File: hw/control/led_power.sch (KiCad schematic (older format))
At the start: 25 parts, among them Q1001 BC807, Q1002 BC817, U801 LM2678T-ADJ

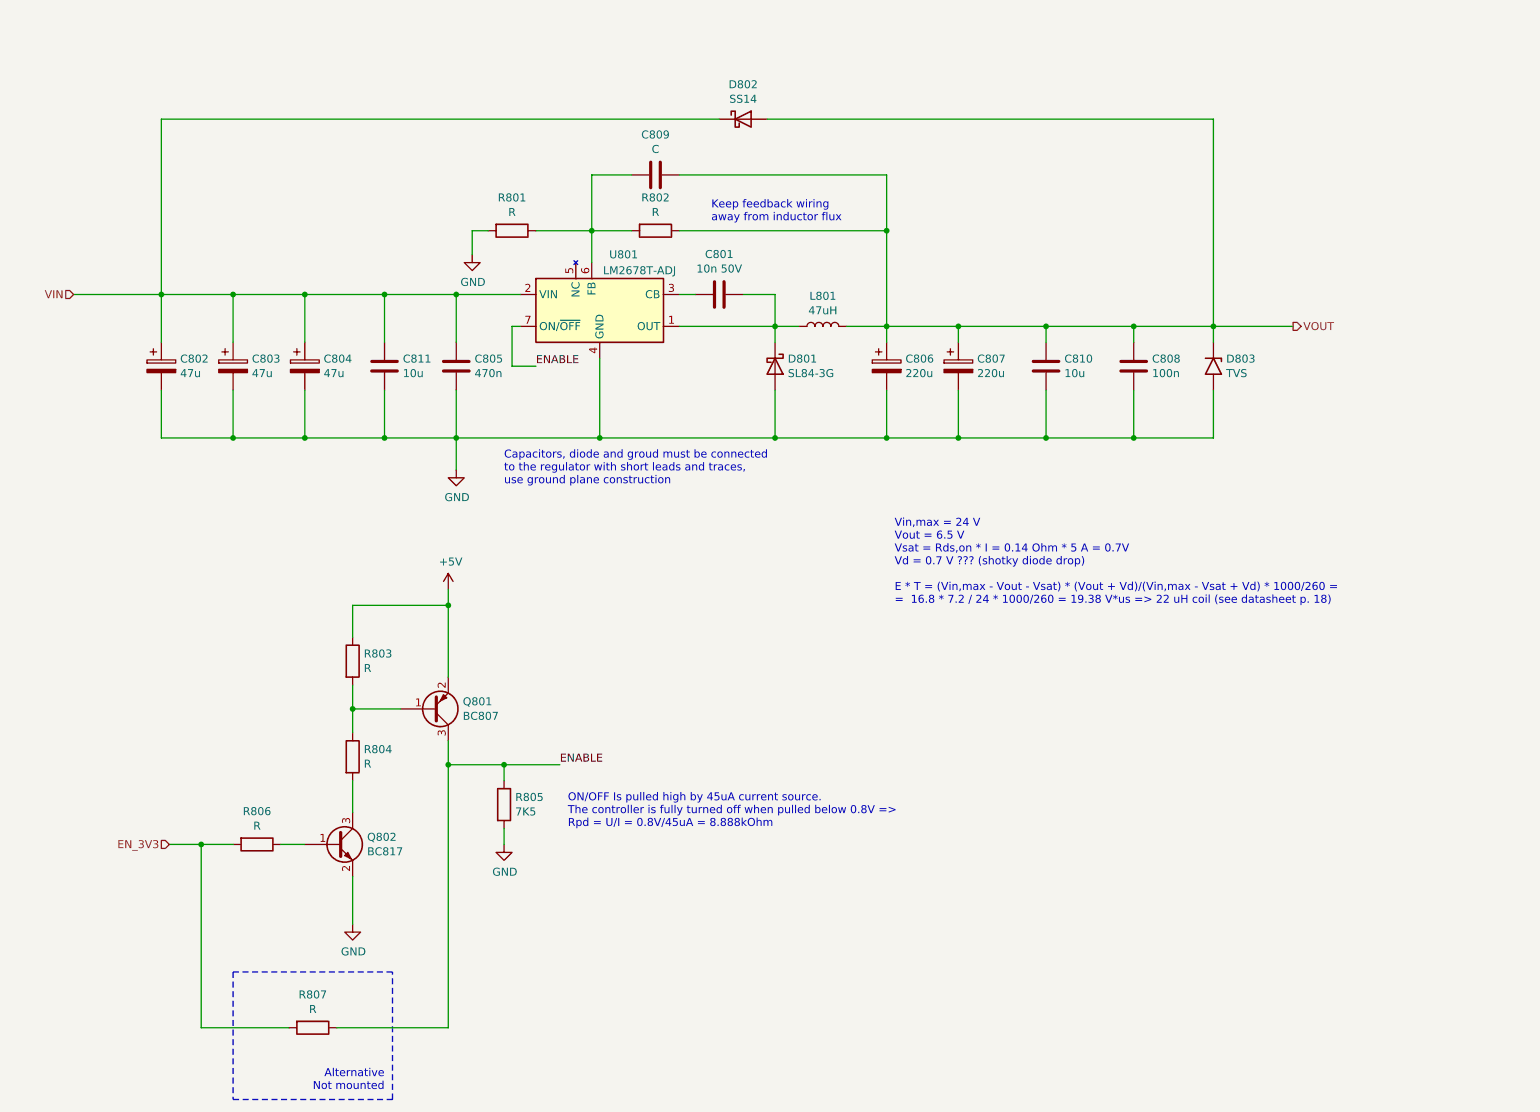
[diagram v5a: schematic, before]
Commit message: [hw] Add 5V supply layout
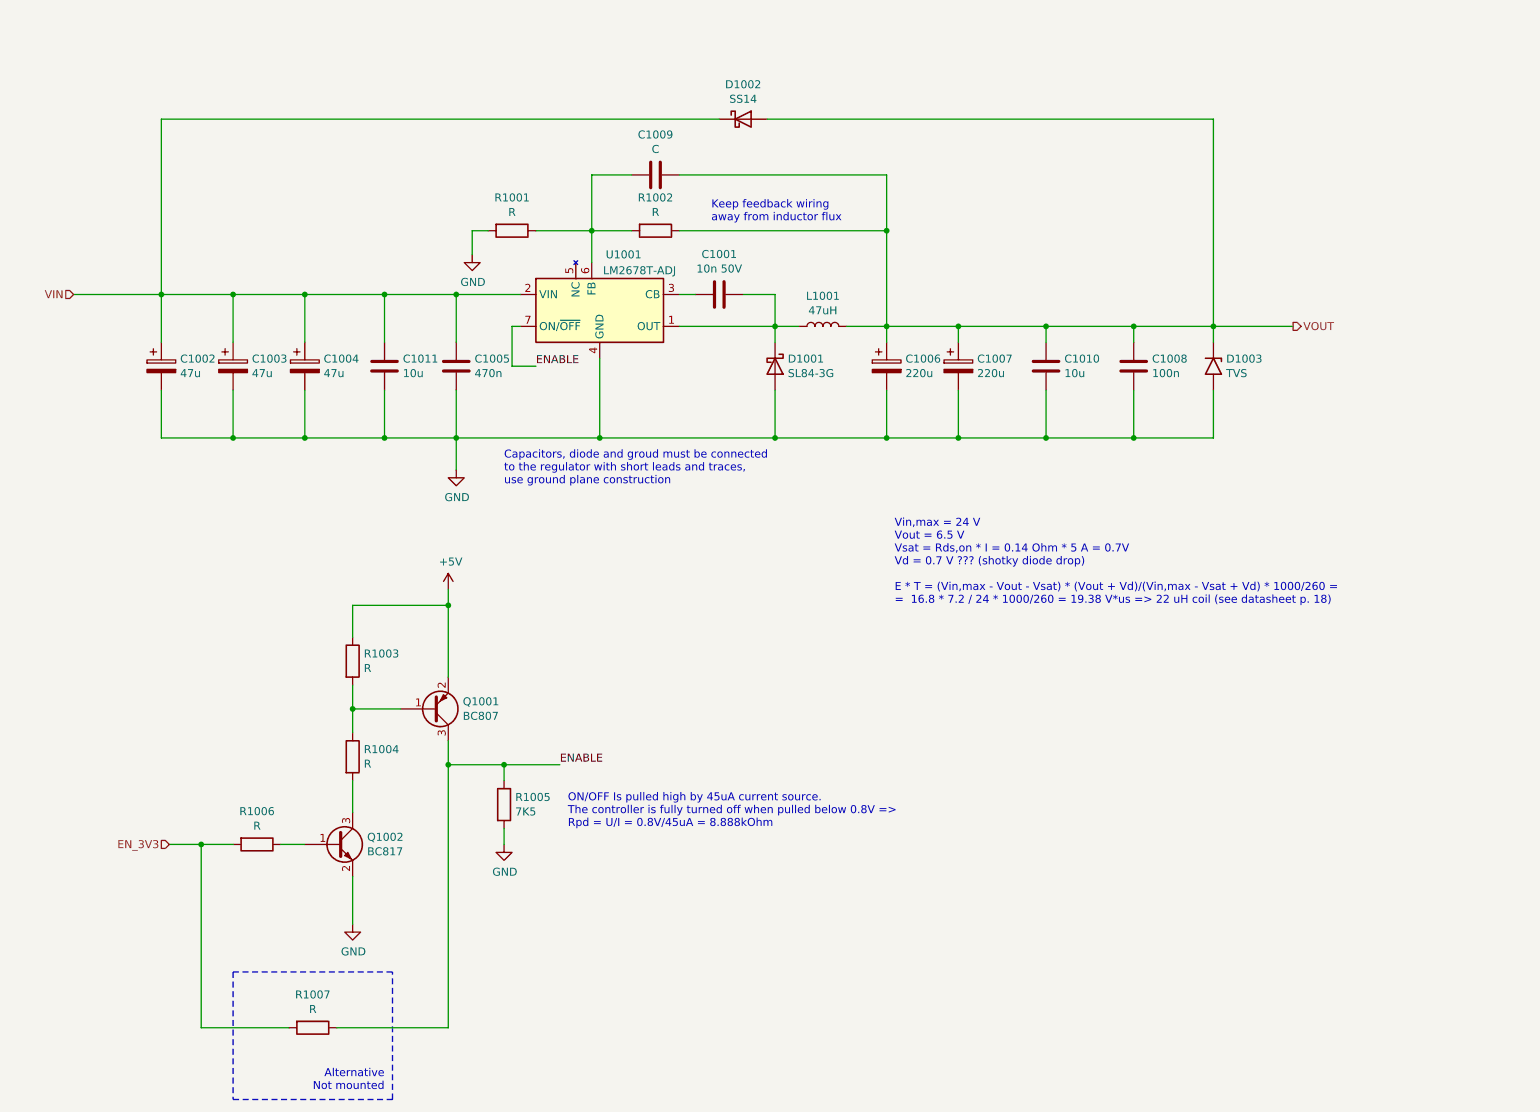
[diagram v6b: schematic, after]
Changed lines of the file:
@@
 AR Path="/614AB031/6145ECF0" Ref="U801"  Part="1"
 AR Path="/614AE8DA/6145ECF0" Ref="U1001"  Part="1"
-F 0 "U801" H 5550 2750 50  0000 C CNN
+F 0 "U1001" H 5550 2750 50  0000 C CNN
 F 1 "LM2678T-ADJ" H 5650 2650 50  0000 C CNN
 F 2 "Package_TO_SOT_THT:TO-220-7_P2.54x3.7mm_StaggerOdd_Lead3.8mm_Vertical" H 5450 2150 50  0001 L CIN
@@
 AR Path="/614AB031/6145FC0F" Ref="C801"  Part="1"
 AR Path="/614AE8DA/6145FC0F" Ref="C1001"  Part="1"
-F 0 "C801" V 5898 2300 50  0000 C CNN
+F 0 "C1001" V 5898 2300 50  0000 C CNN
 F 1 "10n 50V" V 5989 2300 50  0000 C CNN
 F 2 "Capacitor_SMD:C_0805_2012Metric_Pad1.18x1.45mm_HandSolder" H 6188 2150 50  0001 C CNN
@@
 AR Path="/614AB031/61460B18" Ref="#PWR0802"  Part="1"
 AR Path="/614AE8DA/61460B18" Ref="#PWR01002"  Part="1"
-F 0 "#PWR0802" H 4500 3150 50  0001 C CNN
+F 0 "#PWR01002" H 4500 3150 50  0001 C CNN
 F 1 "GND" H 4505 3227 50  0000 C CNN
 F 2 "" H 4500 3400 50  0001 C CNN
@@
 AR Path="/614AE8DA/61461C6E" Ref="D1001"  Part="1"
 AR Path="/614AB031/61461C6E" Ref="D801"  Part="1"
-F 0 "D801" V 6454 2830 50  0000 L CNN
+F 0 "D1001" V 6454 2830 50  0000 L CNN
 F 1 "SL84-3G" V 6545 2830 50  0000 L CNN
 F 2 "Diode_SMD:D_SMC_Handsoldering" H 6500 2750 50  0001 C CNN
@@
 AR Path="/614AE8DA/61462D51" Ref="L1001"  Part="1"
 AR Path="/614AB031/61462D51" Ref="L801"  Part="1"
-F 0 "L801" V 6990 2500 50  0000 C CNN
+F 0 "L1001" V 6990 2500 50  0000 C CNN
 F 1 "47uH" V 6899 2500 50  0000 C CNN
 F 2 "Inductor_THT:L_Toroid_Vertical_L22.4mm_W10.2mm_P7.90mm_Vishay_TJ4" H 6800 2500 50  0001 C CNN
@@
 AR Path="/614AE8DA/61463CC3" Ref="C1006"  Part="1"
 AR Path="/614AB031/61463CC3" Ref="C806"  Part="1"
-F 0 "C806" H 7318 2796 50  0000 L CNN
+F 0 "C1006" H 7318 2796 50  0000 L CNN
 F 1 "220u" H 7318 2705 50  0000 L CNN
 F 2 "Capacitor_THT:CP_Radial_D8.0mm_P3.50mm" H 7238 2600 50  0001 C CNN
@@
 AR Path="/614AE8DA/6146511A" Ref="C1007"  Part="1"
 AR Path="/614AB031/6146511A" Ref="C807"  Part="1"
-F 0 "C807" H 7768 2796 50  0000 L CNN
+F 0 "C1007" H 7768 2796 50  0000 L CNN
 F 1 "220u" H 7768 2705 50  0000 L CNN
 F 2 "Capacitor_THT:CP_Radial_D8.0mm_P3.50mm" H 7688 2600 50  0001 C CNN
@@
 AR Path="/614AE8DA/61465477" Ref="C1004"  Part="1"
 AR Path="/614AB031/61465477" Ref="C804"  Part="1"
-F 0 "C804" H 3668 2796 50  0000 L CNN
+F 0 "C1004" H 3668 2796 50  0000 L CNN
 F 1 "47u" H 3668 2705 50  0000 L CNN
 F 2 "Capacitor_THT:CP_Radial_D8.0mm_P3.50mm" H 3588 2600 50  0001 C CNN
@@
 AR Path="/614AE8DA/614679D1" Ref="C1003"  Part="1"
 AR Path="/614AB031/614679D1" Ref="C803"  Part="1"
-F 0 "C803" H 3218 2796 50  0000 L CNN
+F 0 "C1003" H 3218 2796 50  0000 L CNN
 F 1 "47u" H 3218 2705 50  0000 L CNN
 F 2 "Capacitor_THT:CP_Radial_D8.0mm_P3.50mm" H 3138 2600 50  0001 C CNN
@@
 AR Path="/614AE8DA/61467CFC" Ref="C1002"  Part="1"
 AR Path="/614AB031/61467CFC" Ref="C802"  Part="1"
-F 0 "C802" H 2768 2796 50  0000 L CNN
+F 0 "C1002" H 2768 2796 50  0000 L CNN
 F 1 "47u" H 2768 2705 50  0000 L CNN
 F 2 "Capacitor_THT:CP_Radial_D8.0mm_P3.50mm" H 2688 2600 50  0001 C CNN
@@
 AR Path="/614AE8DA/614681BF" Ref="C1005"  Part="1"
 AR Path="/614AB031/614681BF" Ref="C805"  Part="1"
-F 0 "C805" H 4615 2796 50  0000 L CNN
+F 0 "C1005" H 4615 2796 50  0000 L CNN
 F 1 "470n" H 4615 2705 50  0000 L CNN
 F 2 "Capacitor_SMD:C_0805_2012Metric_Pad1.18x1.45mm_HandSolder" H 4538 2600 50  0001 C CNN
@@
 AR Path="/614AE8DA/6147393D" Ref="R1002"  Part="1"
 AR Path="/614AB031/6147393D" Ref="R802"  Part="1"
-F 0 "R802" V 5543 1900 50  0000 C CNN
+F 0 "R1002" V 5543 1900 50  0000 C CNN
 F 1 "R" V 5634 1900 50  0000 C CNN
 F 2 "Resistor_SMD:R_0805_2012Metric_Pad1.20x1.40mm_HandSolder" V 5680 1900 50  0001 C CNN
@@
 AR Path="/614AE8DA/61475A47" Ref="R1001"  Part="1"
 AR Path="/614AB031/61475A47" Ref="R801"  Part="1"
-F 0 "R801" V 4643 1900 50  0000 C CNN
+F 0 "R1001" V 4643 1900 50  0000 C CNN
 F 1 "R" V 4734 1900 50  0000 C CNN
 F 2 "Resistor_SMD:R_0805_2012Metric_Pad1.20x1.40mm_HandSolder" V 4780 1900 50  0001 C CNN
@@
 AR Path="/614AE8DA/61477A40" Ref="#PWR01001"  Part="1"
 AR Path="/614AB031/61477A40" Ref="#PWR0801"  Part="1"
-F 0 "#PWR0801" H 4600 1800 50  0001 C CNN
+F 0 "#PWR01001" H 4600 1800 50  0001 C CNN
 F 1 "GND" H 4605 1877 50  0000 C CNN
 F 2 "" H 4600 2050 50  0001 C CNN
@@
 AR Path="/614AE8DA/6147DB7E" Ref="R1006"  Part="1"
 AR Path="/614AB031/6147DB7E" Ref="R806"  Part="1"
-F 0 "R806" V 3043 5750 50  0000 C CNN
+F 0 "R1006" V 3043 5750 50  0000 C CNN
 F 1 "R" V 3134 5750 50  0000 C CNN
 F 2 "Resistor_SMD:R_0805_2012Metric_Pad1.20x1.40mm_HandSolder" V 3180 5750 50  0001 C CNN
@@
 AR Path="/614AE8DA/6147EFCD" Ref="Q1002"  Part="1"
 AR Path="/614AB031/6147EFCD" Ref="Q802"  Part="1"
-F 0 "Q802" H 3941 5796 50  0000 L CNN
+F 0 "Q1002" H 3941 5796 50  0000 L CNN
 F 1 "BC817" H 3941 5705 50  0000 L CNN
 F 2 "Package_TO_SOT_SMD:SOT-23_Handsoldering" H 3950 5850 50  0001 C CNN
@@
 AR Path="/614AE8DA/61480A0D" Ref="Q1001"  Part="1"
 AR Path="/614AB031/61480A0D" Ref="Q801"  Part="1"
-F 0 "Q801" H 4541 4854 50  0000 L CNN
+F 0 "Q1001" H 4541 4854 50  0000 L CNN
 F 1 "BC807" H 4541 4945 50  0000 L CNN
 F 2 "Package_TO_SOT_SMD:SOT-23_Handsoldering" H 4550 5000 50  0001 C CNN
@@
 AR Path="/614AE8DA/6148128F" Ref="R1004"  Part="1"
 AR Path="/614AB031/6148128F" Ref="R804"  Part="1"
-F 0 "R804" H 3920 5246 50  0000 L CNN
+F 0 "R1004" H 3920 5246 50  0000 L CNN
 F 1 "R" H 3920 5155 50  0000 L CNN
 F 2 "Resistor_SMD:R_0805_2012Metric_Pad1.20x1.40mm_HandSolder" V 3780 5200 50  0001 C CNN
@@
 AR Path="/614AE8DA/614817B0" Ref="R1003"  Part="1"
 AR Path="/614AB031/614817B0" Ref="R803"  Part="1"
-F 0 "R803" H 3920 4646 50  0000 L CNN
+F 0 "R1003" H 3920 4646 50  0000 L CNN
 F 1 "R" H 3920 4555 50  0000 L CNN
 F 2 "Resistor_SMD:R_0805_2012Metric_Pad1.20x1.40mm_HandSolder" V 3780 4600 50  0001 C CNN
@@
 AR Path="/614AE8DA/61483286" Ref="#PWR01004"  Part="1"
 AR Path="/614AB031/61483286" Ref="#PWR0804"  Part="1"
-F 0 "#PWR0804" H 3850 6000 50  0001 C CNN
+F 0 "#PWR01004" H 3850 6000 50  0001 C CNN
 F 1 "GND" H 3855 6077 50  0000 C CNN
 F 2 "" H 3850 6250 50  0001 C CNN
@@
 AR Path="/614AE8DA/61486663" Ref="#PWR01003"  Part="1"
 AR Path="/614AB031/61486663" Ref="#PWR0803"  Part="1"
-F 0 "#PWR0803" H 4450 4000 50  0001 C CNN
+F 0 "#PWR01003" H 4450 4000 50  0001 C CNN
 F 1 "+5V" H 4465 4323 50  0000 C CNN
 F 2 "" H 4450 4150 50  0001 C CNN
@@
 AR Path="/614AE8DA/6148D73D" Ref="R1005"  Part="1"
 AR Path="/614AB031/6148D73D" Ref="R805"  Part="1"
-F 0 "R805" H 4870 5546 50  0000 L CNN
+F 0 "R1005" H 4870 5546 50  0000 L CNN
 F 1 "7K5" H 4870 5455 50  0000 L CNN
 F 2 "Resistor_SMD:R_0805_2012Metric_Pad1.20x1.40mm_HandSolder" V 4730 5500 50  0001 C CNN
@@
 AR Path="/614AE8DA/614CC1BE" Ref="R1007"  Part="1"
 AR Path="/614AB031/614CC1BE" Ref="R807"  Part="1"
-F 0 "R807" V 3393 6900 50  0000 C CNN
+F 0 "R1007" V 3393 6900 50  0000 C CNN
 F 1 "R" V 3484 6900 50  0000 C CNN
 F 2 "Resistor_SMD:R_0805_2012Metric_Pad1.20x1.40mm_HandSolder" V 3530 6900 50  0001 C CNN
@@
 AR Path="/614AB031/6169A3CC" Ref="C808"  Part="1"
 AR Path="/614AE8DA/6169A3CC" Ref="C1008"  Part="1"
-F 0 "C808" H 8865 2796 50  0000 L CNN
+F 0 "C1008" H 8865 2796 50  0000 L CNN
 F 1 "100n" H 8865 2705 50  0000 L CNN
 F 2 "Capacitor_SMD:C_0805_2012Metric_Pad1.18x1.45mm_HandSolder" H 8788 2600 50  0001 C CNN
@@
 AR Path="/614AB031/616AD78A" Ref="C809"  Part="1"
 AR Path="/614AE8DA/616AD78A" Ref="C1009"  Part="1"
-F 0 "C809" V 5498 1550 50  0000 C CNN
+F 0 "C1009" V 5498 1550 50  0000 C CNN
 F 1 "C" V 5589 1550 50  0000 C CNN
 F 2 "Capacitor_SMD:C_0805_2012Metric_Pad1.18x1.45mm_HandSolder" H 5788 1400 50  0001 C CNN
@@
 AR Path="/614AB031/616C4247" Ref="D803"  Part="1"
 AR Path="/614AE8DA/616C4247" Ref="D1003"  Part="1"
-F 0 "D803" V 9204 2830 50  0000 L CNN
+F 0 "D1003" V 9204 2830 50  0000 L CNN
 F 1 "TVS" V 9295 2830 50  0000 L CNN
 F 2 "Diode_SMD:D_SMA_Handsoldering" H 9250 2550 50  0001 C CNN
@@
 AR Path="/614AB031/616CF895" Ref="#PWR0805"  Part="1"
 AR Path="/614AE8DA/616CF895" Ref="#PWR01005"  Part="1"
-F 0 "#PWR0805" H 4800 5500 50  0001 C CNN
+F 0 "#PWR01005" H 4800 5500 50  0001 C CNN
 F 1 "GND" H 4805 5577 50  0000 C CNN
 F 2 "" H 4800 5750 50  0001 C CNN
@@
 AR Path="/614AB031/617136B8" Ref="C810"  Part="1"
 AR Path="/614AE8DA/617136B8" Ref="C1010"  Part="1"
-F 0 "C810" H 8315 2796 50  0000 L CNN
+F 0 "C1010" H 8315 2796 50  0000 L CNN
 F 1 "10u" H 8315 2705 50  0000 L CNN
 F 2 "Capacitor_SMD:C_1210_3225Metric_Pad1.33x2.70mm_HandSolder" H 8238 2600 50  0001 C CNN
@@
 AR Path="/614AB031/61725C25" Ref="C811"  Part="1"
 AR Path="/614AE8DA/61725C25" Ref="C1011"  Part="1"
-F 0 "C811" H 4165 2796 50  0000 L CNN
+F 0 "C1011" H 4165 2796 50  0000 L CNN
 F 1 "10u" H 4165 2705 50  0000 L CNN
 F 2 "Capacitor_SMD:C_1210_3225Metric_Pad1.33x2.70mm_HandSolder" H 4088 2600 50  0001 C CNN
@@
 AR Path="/614AB031/616C93E8" Ref="D802"  Part="1"
 AR Path="/614AE8DA/616C93E8" Ref="D1002"  Part="1"
-F 0 "D802" H 6300 1417 50  0000 C CNN
+F 0 "D1002" H 6300 1417 50  0000 C CNN
 F 1 "SS14" H 6300 1326 50  0000 C CNN
 F 2 "Diode_SMD:D_SMA-SMB_Universal_Handsoldering" H 6300 1200 50  0001 C CNN
